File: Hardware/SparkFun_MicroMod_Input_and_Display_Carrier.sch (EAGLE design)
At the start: 59 parts, among them J1 MICROMOD-2222-C, J2 MICRO-SD, J3 USB-C_Prog, J4 AVR_SPI_PROG_3X2TESTPOINTS, J5 2.4" TFT, J6 QWIIC_RIGHT_ANGLE, Q1 1.1A/60V/600mΩ, U2 ATTINY84, U5 AP7361C-33FGE

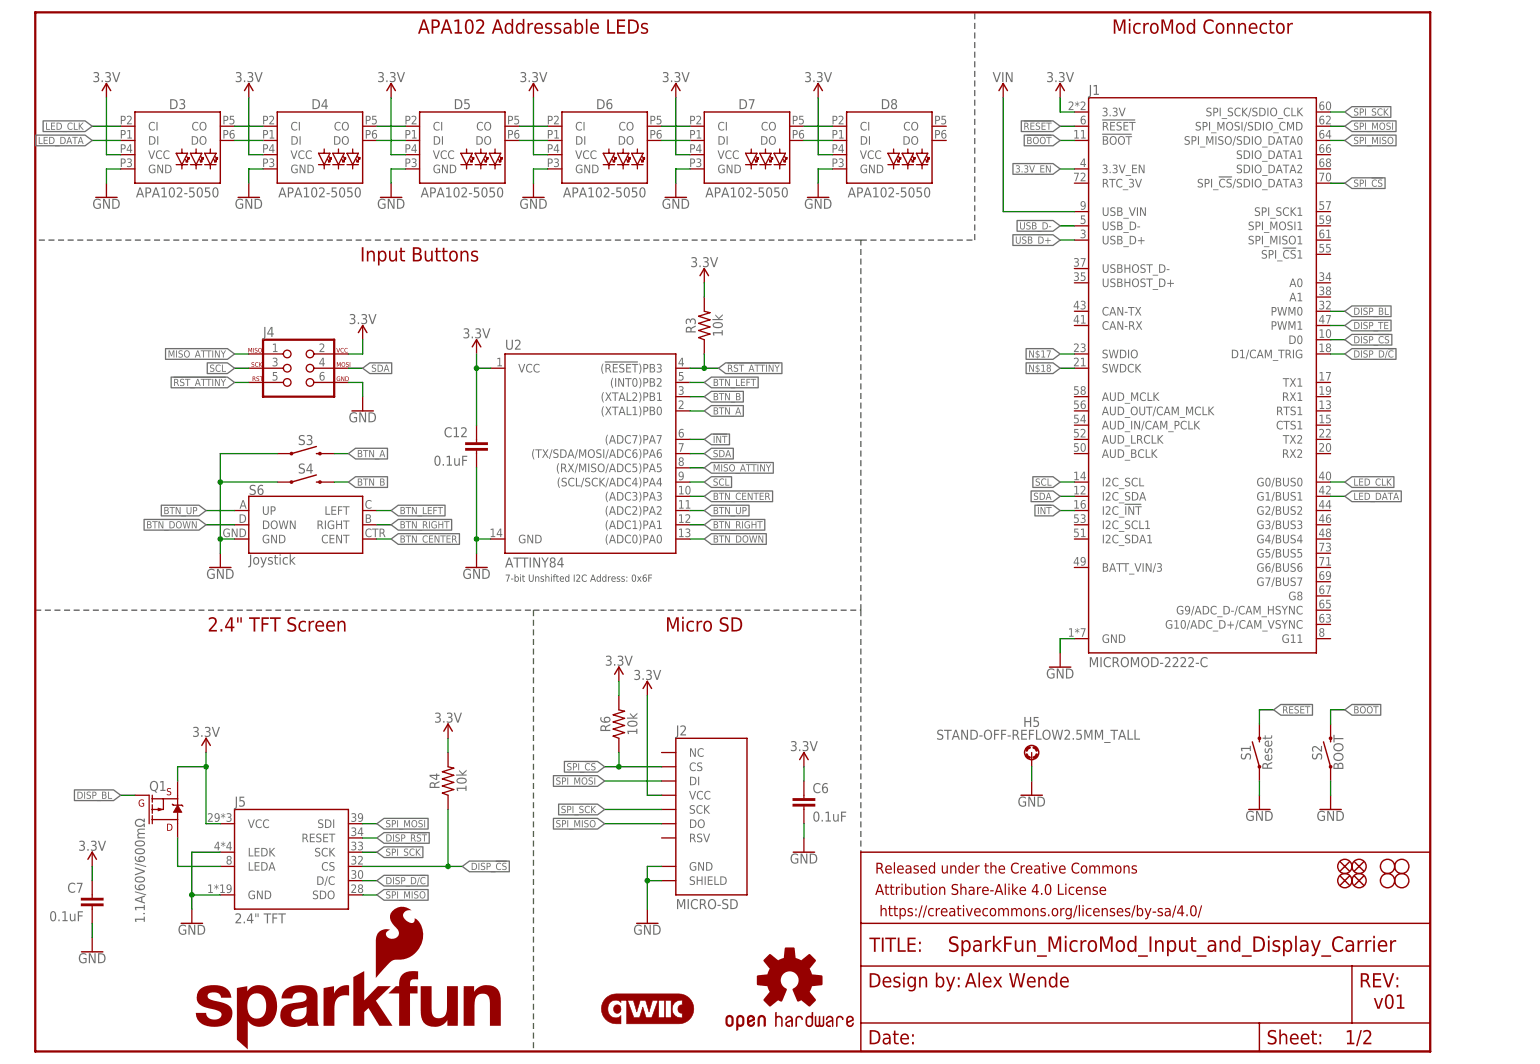
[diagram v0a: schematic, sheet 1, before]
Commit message: Pre-review changes
Added SWD connector
Updated SPI names
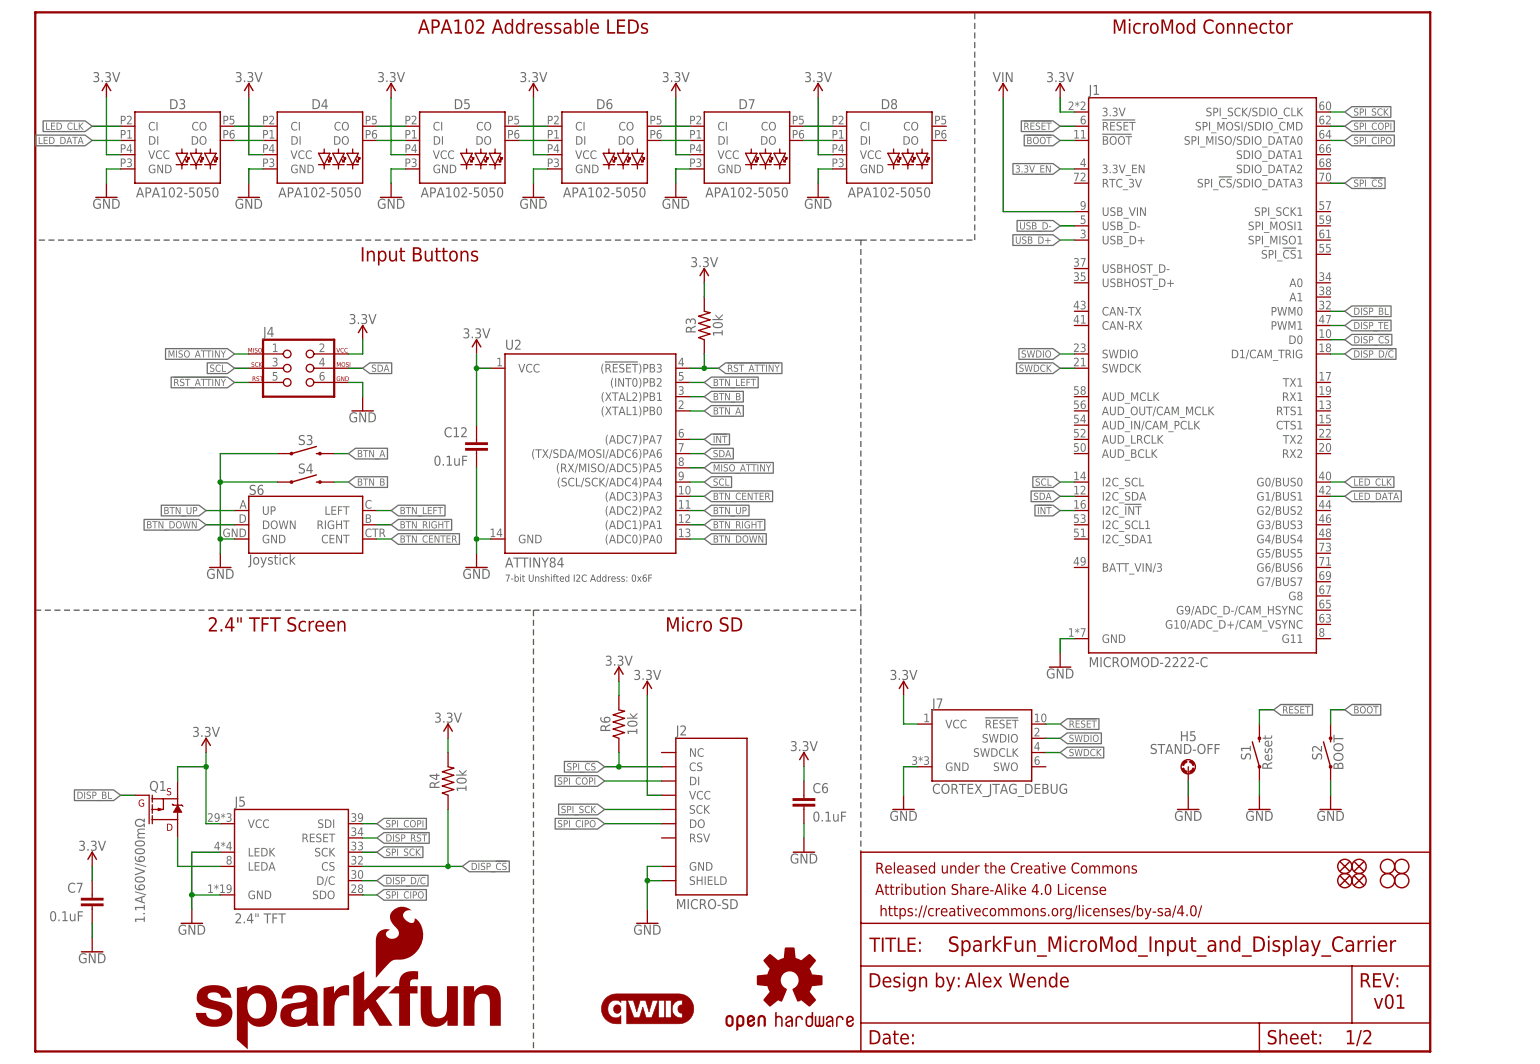
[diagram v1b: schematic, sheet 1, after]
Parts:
- added J7: CORTEX_JTAG_DEBUG, SparkFun-Connectors:CORTEX_JTAG_DEBUG_MINIMUM_PTH_NS
- H5: value STAND-OFF-REFLOW2.5MM_TALL -> STAND-OFF
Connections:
- net SPI_MISO renamed SPI_CIPO
- net SPI_MOSI renamed SPI_COPI
- removed net N$17: J1.SWDIO
- removed net N$18: J1.SWDCK
- new net SWDCK: J1.SWDCK, J7.SWDCLK
- new net SWDIO: J1.SWDIO, J7.SWDIO
- net !RESET: now also J7.!RESET
- net 3.3V: now also J7.VCC
- net GND: now also J7.GND
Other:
- moved on the sheet: H5
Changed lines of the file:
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@@
 <?xml version="1.0" encoding="utf-8"?>
 <!DOCTYPE eagle SYSTEM "eagle.dtd">
-<eagle version="9.6.0">
+<eagle version="9.5.2">
 <drawing>
 <settings>
@@
 <layer number="255" name="routoute" color="7" fill="1" visible="no" active="no"/>
 </layers>
-<schematic xreflabel="%F%N/%S" xrefpart="1_/%S.%C%R">
+<schematic xreflabel="%F%N/%S" xrefpart="/%S.%C%R">
 <attributes>
 </attributes>
@@
 <part name="GND15" library="SparkFun-PowerSymbols" deviceset="GND" device=""/>
 <part name="GND19" library="SparkFun-PowerSymbols" deviceset="GND" device=""/>
-<part name="H5" library="SparkFun-Hardware" deviceset="STAND-OFF-REFLOW" device="2.5MM_TALL"/>
+<part name="H5" library="SparkFun-Hardware" deviceset="STAND-OFF-REFLOW" device="2.5MM_TALL" value="STAND-OFF"/>
 <part name="J3" library="SparkFun-Connectors" deviceset="USB_C" device="_2-LAYER_PADS" value="USB-C_Prog"/>
 <part name="SUPPLY4" library="SparkFun-PowerSymbols" deviceset="V_USB" device=""/>
@@
 <part name="LOGO2" library="SparkFun-Aesthetics" deviceset="QWIIC_LOGO" device="_5MM"/>
 <part name="LOGO3" library="SparkFun-Aesthetics" deviceset="OSHW-LOGO" device="S" value="OSHW-LOGOS"/>
+<part name="J7" library="SparkFun-Connectors" deviceset="CORTEX_JTAG_DEBUG_MINIMUM" device="_PTH_NS" value="CORTEX_JTAG_DEBUG"/>
+<part name="SUPPLY25" library="SparkFun-PowerSymbols" deviceset="3.3V" device=""/>
+<part name="GND31" library="SparkFun-PowerSymbols" deviceset="GND" device=""/>
 </parts>
 <sheets>
@@
 <attribute name="VALUE" x="231.14" y="42.926" size="1.778" layer="96" rot="MR0" align="top-center"/>
 </instance>
-<instance part="GND19" gate="1" x="177.8" y="45.72" smashed="yes">
-<attribute name="VALUE" x="177.8" y="45.466" size="1.778" layer="96" align="top-center"/>
-</instance>
-<instance part="H5" gate="G$1" x="177.8" y="53.34" smashed="yes">
-<attribute name="NAME" x="176.276" y="57.912" size="1.778" layer="95"/>
-<attribute name="VALUE" x="160.782" y="55.626" size="1.778" layer="96"/>
+<instance part="GND19" gate="1" x="205.74" y="43.18" smashed="yes">
+<attribute name="VALUE" x="205.74" y="42.926" size="1.778" layer="96" align="top-center"/>
+</instance>
+<instance part="H5" gate="G$1" x="205.74" y="50.8" smashed="yes">
+<attribute name="NAME" x="204.216" y="55.372" size="1.778" layer="95"/>
+<attribute name="VALUE" x="198.882" y="53.086" size="1.778" layer="96"/>
 </instance>
 <instance part="GND1" gate="1" x="182.88" y="68.58" smashed="yes">
@@
 <instance part="LOGO2" gate="G$1" x="109.22" y="7.62" smashed="yes"/>
 <instance part="LOGO3" gate="G$1" x="134.62" y="12.7" smashed="yes"/>
+<instance part="J7" gate="G$1" x="170.18" y="53.34" smashed="yes">
+<attribute name="NAME" x="160.02" y="61.214" size="1.778" layer="95" font="vector"/>
+<attribute name="VALUE" x="160.02" y="45.974" size="1.778" layer="96" font="vector"/>
+</instance>
+<instance part="SUPPLY25" gate="G$1" x="154.94" y="63.5" smashed="yes">
+<attribute name="VALUE" x="154.94" y="66.294" size="1.778" layer="96" align="bottom-center"/>
+</instance>
+<instance part="GND31" gate="1" x="154.94" y="43.18" smashed="yes">
+<attribute name="VALUE" x="154.94" y="42.926" size="1.778" layer="96" align="top-center"/>
+</instance>
 </instances>
 <busses>
@@
 </segment>
 </net>
-<net name="SPI_MOSI" class="0">
+<net name="SPI_COPI" class="0">
 <segment>
 <pinref part="J1" gate="J1" pin="SPI_MOSI/SDIO_CMD"/>
@@
 </segment>
 </net>
-<net name="SPI_MISO" class="0">
+<net name="SPI_CIPO" class="0">
 <segment>
 <pinref part="J1" gate="J1" pin="SPI_MISO/SDIO_DATA0"/>
@@
 <label x="220.98" y="60.96" size="1.27" layer="95" xref="yes"/>
 </segment>
+<segment>
+<pinref part="J7" gate="G$1" pin="!RESET"/>
+<wire x1="180.34" y1="58.42" x2="182.88" y2="58.42" width="0.1524" layer="91"/>
+<label x="182.88" y="58.42" size="1.27" layer="95" xref="yes"/>
+</segment>
 </net>
 <net name="!BOOT" class="0">
@@
 </segment>
 </net>
-<net name="N$17" class="0">
-<segment>
-<pinref part="J1" gate="J1" pin="SWDIO"/>
-<wire x1="185.42" y1="124.46" x2="182.88" y2="124.46" width="0.1524" layer="91"/>
-<label x="182.88" y="124.46" size="1.27" layer="95" rot="R180" xref="yes"/>
-</segment>
-</net>
-<net name="N$18" class="0">
-<segment>
-<pinref part="J1" gate="J1" pin="SWDCK"/>
-<wire x1="185.42" y1="121.92" x2="182.88" y2="121.92" width="0.1524" layer="91"/>
-<label x="182.88" y="121.92" size="1.27" layer="95" rot="R180" xref="yes"/>
-</segment>
-</net>
 <net name="GND" class="0">
 <segment>
@@
 <segment>
 <pinref part="GND19" gate="1" pin="GND"/>
-<wire x1="177.8" y1="48.26" x2="177.8" y2="50.8" width="0.1524" layer="91"/>
+<wire x1="205.74" y1="45.72" x2="205.74" y2="48.26" width="0.1524" layer="91"/>
 <pinref part="H5" gate="G$1" pin="1"/>
 </segment>
@@
 <pinref part="GND30" gate="1" pin="GND"/>
 </segment>
+<segment>
+<pinref part="J7" gate="G$1" pin="GND"/>
+<wire x1="157.48" y1="50.8" x2="154.94" y2="50.8" width="0.1524" layer="91"/>
+<wire x1="154.94" y1="50.8" x2="154.94" y2="45.72" width="0.1524" layer="91"/>
+<pinref part="GND31" gate="1" pin="GND"/>
+</segment>
 </net>
 <net name="3.3V" class="0">
@@
 <pinref part="SUPPLY5" gate="G$1" pin="3.3V"/>
 </segment>
+<segment>
+<pinref part="J7" gate="G$1" pin="VCC"/>
+<wire x1="157.48" y1="58.42" x2="154.94" y2="58.42" width="0.1524" layer="91"/>
+<wire x1="154.94" y1="58.42" x2="154.94" y2="63.5" width="0.1524" layer="91"/>
+<pinref part="SUPPLY25" gate="G$1" pin="3.3V"/>
+</segment>
 </net>
 <net name="USB_D-" class="0">
@@
 </segment>
 </net>
+<net name="SWDIO" class="0">
+<segment>
+<pinref part="J7" gate="G$1" pin="SWDIO"/>
+<wire x1="180.34" y1="55.88" x2="182.88" y2="55.88" width="0.1524" layer="91"/>
+<label x="182.88" y="55.88" size="1.27" layer="95" xref="yes"/>
+</segment>
+<segment>
+<pinref part="J1" gate="J1" pin="SWDIO"/>
+<wire x1="185.42" y1="124.46" x2="182.88" y2="124.46" width="0.1524" layer="91"/>
+<label x="182.88" y="124.46" size="1.27" layer="95" rot="R180" xref="yes"/>
+</segment>
+</net>
+<net name="SWDCK" class="0">
+<segment>
+<pinref part="J7" gate="G$1" pin="SWDCLK"/>
+<wire x1="180.34" y1="53.34" x2="182.88" y2="53.34" width="0.1524" layer="91"/>
+<label x="182.88" y="53.34" size="1.27" layer="95" xref="yes"/>
+</segment>
+<segment>
+<pinref part="J1" gate="J1" pin="SWDCK"/>
+<wire x1="185.42" y1="121.92" x2="182.88" y2="121.92" width="0.1524" layer="91"/>
+<label x="182.88" y="121.92" size="1.27" layer="95" rot="R180" xref="yes"/>
+</segment>
+</net>

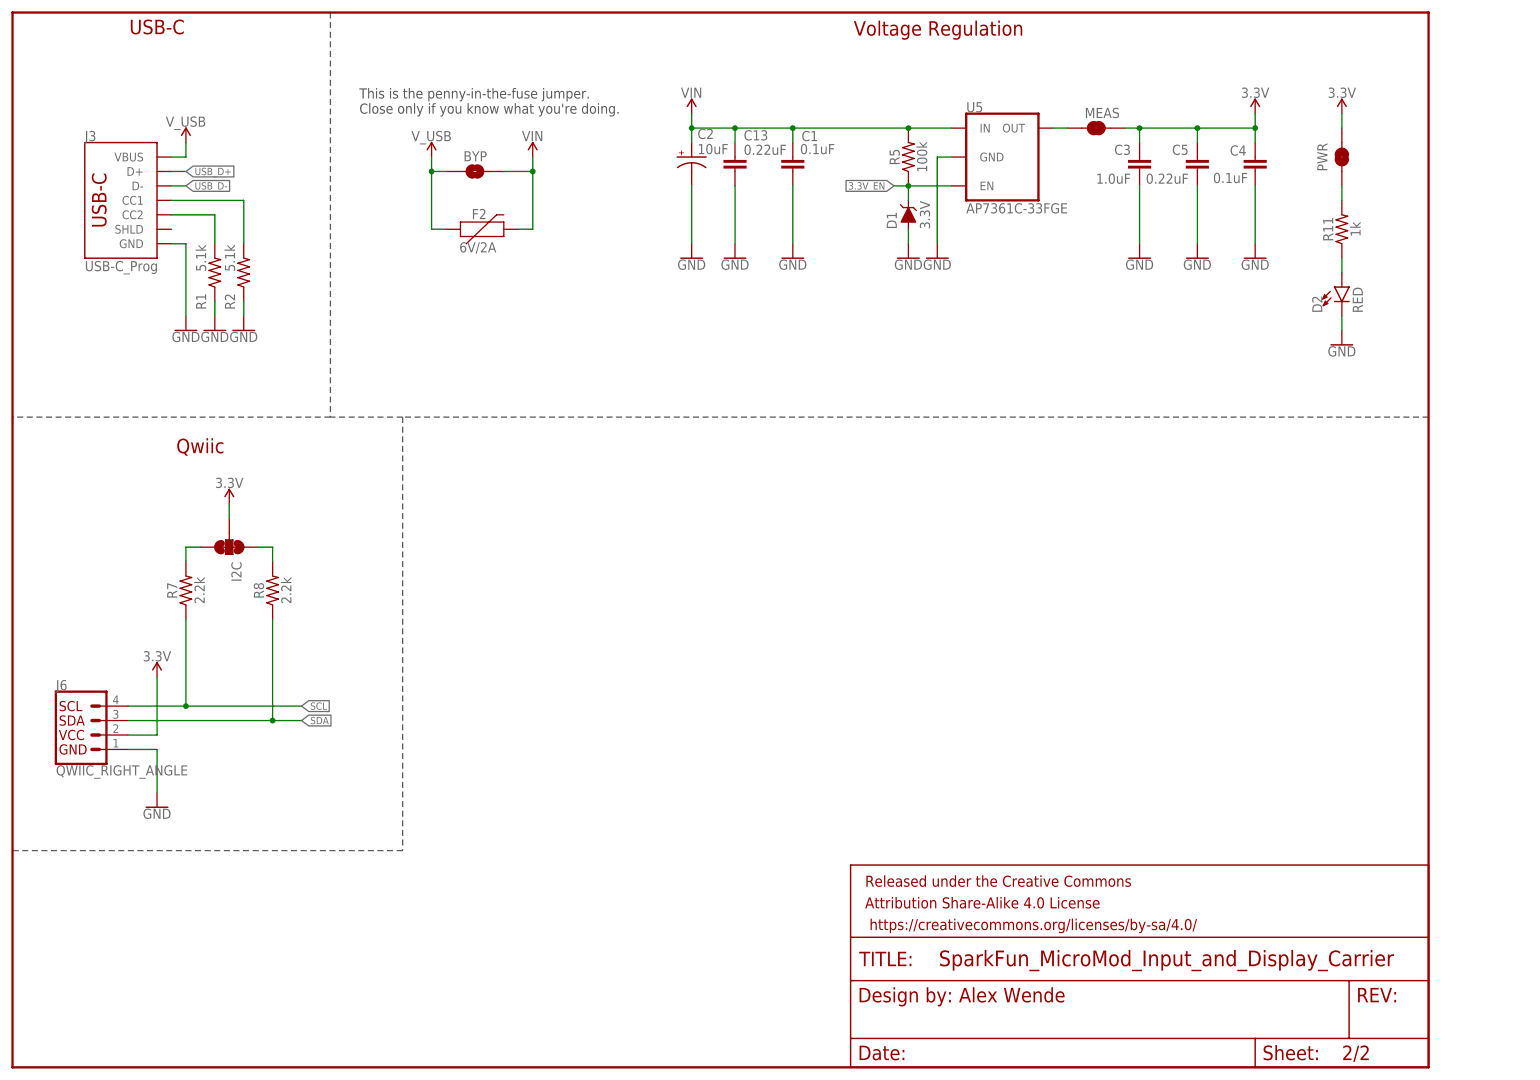
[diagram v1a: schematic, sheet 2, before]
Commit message: Post review changes
- Added notes for jumpers
- Changed SPI_CS to SD_CS label
- Connected display reset to IO
- Added NO jumper between MicroMod and regulator enable
- Added Buzzer to PWM1
- Broke out A0/1, RX1/TX1, CAN-RX/TX, 3.3V, and GND
- Added name on back of the board
- Fixed or corrected DRC errors
- Fixed non-mitered corners
- Moved reset and boot buttons
- Added indicator for "UP" on 5-way switch
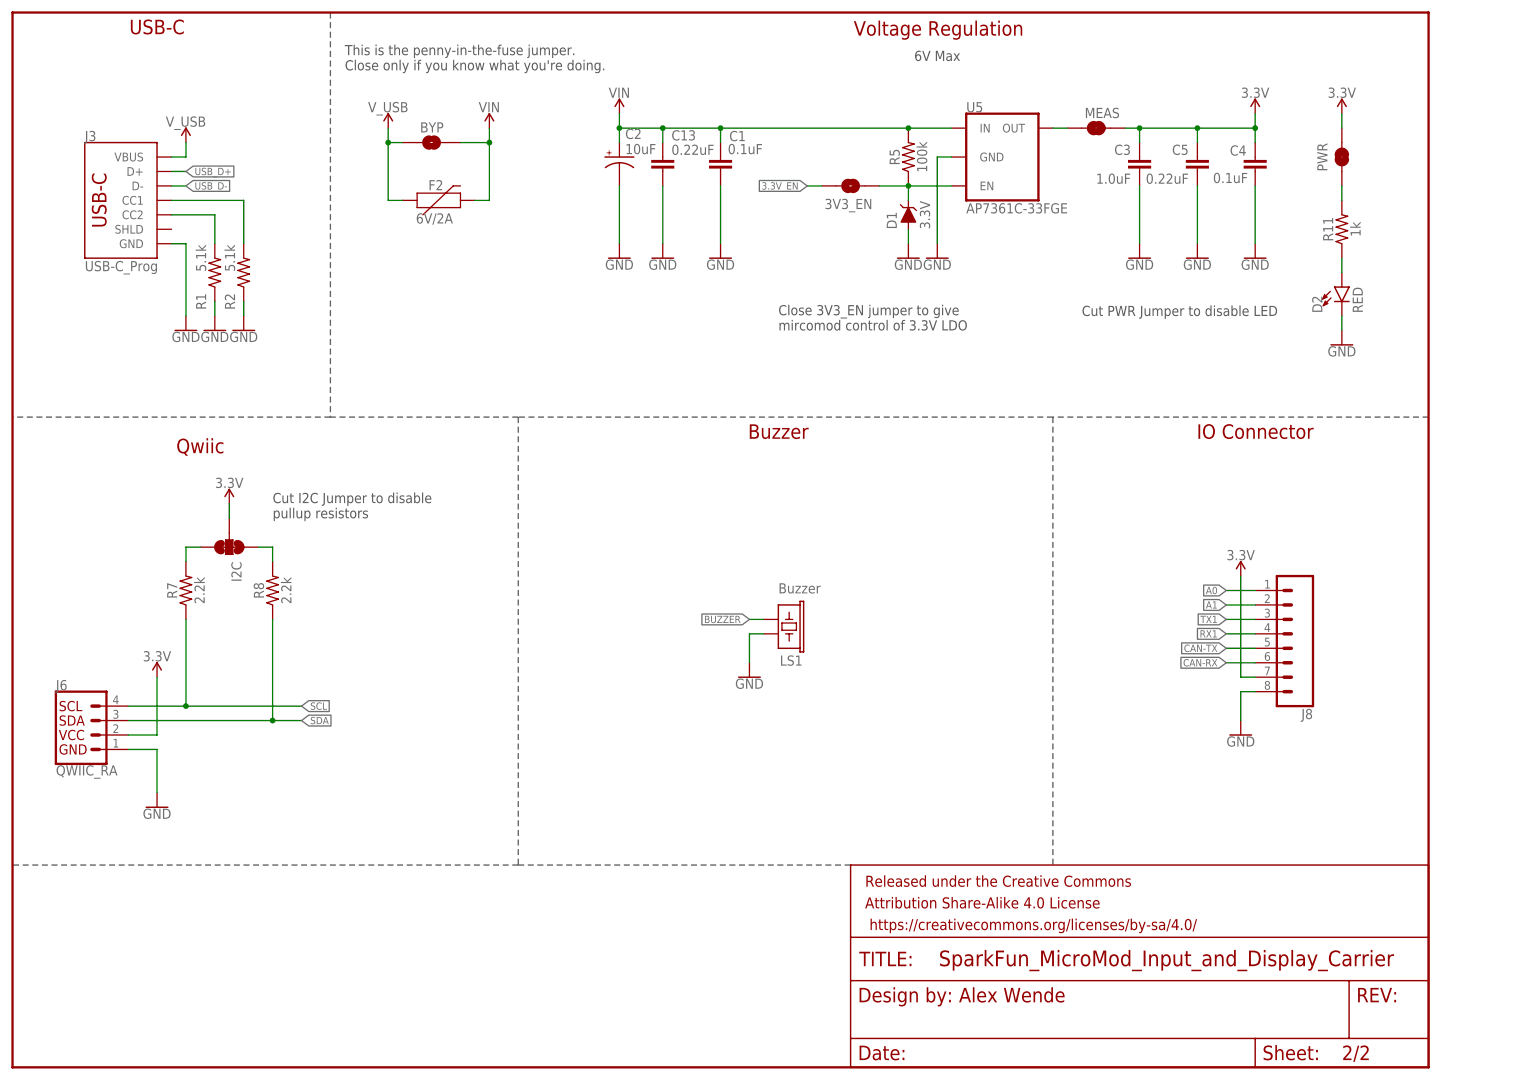
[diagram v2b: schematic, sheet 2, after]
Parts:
- added 3V3_EN: JUMPER-SMT_2_NO_SILK, SparkFun-Jumpers:JUMPER-SMT_2_NO_SILK
- added J8: (no value), SparkFun-Connectors:CONN_08NO_SILK_DNP
- added LS1: Buzzer, SparkFun-Electromechanical:BUZZER-SMD
- added R9: 10k, SparkFun-Resistors:10KOHM-0603-1/10W-1%
- J6: value QWIIC_RIGHT_ANGLE -> QWIIC_RA
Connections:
- net SPI_!CS renamed SD_!CS
- removed net DISP_TE: J1.PWM1
- new net A0: J1.A0, J8.1
- new net A1: J1.A1, J8.2
- new net BUZZER: J1.PWM1, LS1.2
- new net CAN-RX: J1.CAN-RX, J8.6
- new net CAN-TX: J1.CAN-TX, J8.5
- new net ENABLE: 3V3_EN.2, D1.C, R5.1, U5.EN
- new net RX1: J1.RX1, J8.4
- new net TX1: J1.TX1, J8.3
- net 3.3V: now also J8.7
- net 3.3V_EN: now also 3V3_EN.1; no longer D1.C, R5.1, U5.EN
- net DISP_!RST: now also J1.G2/BUS2
- net DISP_BL: now also R9.2
- net GND: now also J8.8, LS1.1, R9.1
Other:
- note added: "6V Max"
- note added: "Buzzer"
- note added: "Close 3V3_EN jumper to give mircomod control of 3.3V LDO"
- note added: "Cut I2C Jumper to disable pullup resistors"
- note added: "Cut PWR Jumper to disable LED"
- note added: "IO Connector"
- moved on the sheet: BYP, C1, C13, C2, C7, F2
